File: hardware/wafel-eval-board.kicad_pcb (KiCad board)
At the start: 2 copper layers, 262 parts, among them J101 CAN PORT, J102 SW, J201 Conn_01x02, J202 Conn_01x02, J203 Conn_01x02, J204 Conn_01x02, J205 Conn_01x02, J801 UART1, Q1001 DMG2302UK, Q101 AO3422, Q1101 DMG2302UK, Q1201 DMG2302UK, Q1301 DMG2302UK, Q1401 DMG2302UK, Q1501 DMG2302UK, Q1601 DMG2302UK, Q1701 DMG2302UK, Q1801 DMG2302UK, Q1901 DMG2302UK, Q201 NPN, Q202 DMG2302UK, Q301 IRLML6402, Q302 DMG2302UK, Q401 IPB085N15NM6, Q402 IPB085N15NM6, Q403 IPB085N15NM6, Q501 IPB085N15NM6, Q502 IPB085N15NM6, Q503 IPB085N15NM6, Q601 IRFR9024, Q701 IRFR9024, Q901 ZXMP10A13FTA, Q902 DMG2302UK, SW801 SW_Push, U101 LM5163DDA, U201 BQ7694204, U801 NUCLEO-L432KC, U802 TCAN1043A, U803 TLP241A

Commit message: ADD ZONES
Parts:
- moved D701 5.39 mm to (198.8, 75.7)
- moved R701 5.39 mm to (199.1, 72.7)
- moved D601 0.76 mm to (199.6, 90.9)
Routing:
- added copper zone on B.Cu, net (none)
- added copper zone on F.Cu, net (none)
- added copper zone on B.Cu, net /BAT+
- added copper zone on F.Cu, net /BAT+
- added copper zone on B.Cu, net /CH
- added copper zone on F.Cu, net /CH
- added copper zone on B.Cu, net /PACK+
- added copper zone on F.Cu, net /PACK+
- added copper zone on B.Cu, net PGND
- added copper zone on F.Cu, net PGND
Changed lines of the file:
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@@
 	(footprint "Diode_SMD:D_SOD-123F"
 		(layer "F.Cu")
-		(at 198.7804 81.1052 -90)
+		(at 198.7804 75.7144 -90)
 		(descr "D_SOD-123F")
 		(tags "D_SOD-123F")
@@
 	(footprint "Diode_SMD:D_SOD-123F"
 		(layer "F.Cu")
-		(at 198.882 90.8528 90)
+		(at 199.644 90.9036 90)
 		(descr "D_SOD-123F")
 		(tags "D_SOD-123F")
@@
 	(footprint "Resistor_SMD:R_0603_1608Metric"
 		(layer "F.Cu")
-		(at 199.1238 78.1304)
+		(at 199.1238 72.7396)
 		(descr "Resistor SMD 0603 (1608 Metric), square (rectangular) end terminal, IPC-7351 nominal, (Body size source: IPC-SM-782 page 72, https://www.pcb-3d.com/wordpress/wp-content/uploads/ipc-sm-782a_amendment_1_and_2.pdf)")
 		(tags "resistor")
@@
 	)
 	(zone
+		(net "/BAT+")
+		(layers "F.Cu" "B.Cu")
+		(name "PW_BAT+")
+		(hatch edge 0.5)
+		(priority 1)
+		(connect_pads
+			(clearance 0)
+		)
+		(min_thickness 0.25)
+		(fill
+			(thermal_gap 0.5)
+			(thermal_bridge_width 0.5)
+			(island_removal_mode 1)
+		)
+		(polygon
+			(pts
+				(xy 197.293326 92.960718) (xy 197.188993 137.321792) (xy 268.792701 137.512549) (xy 268.910981 93.17037)
+			)
+		)
+	)
+	(zone
+		(net "/PACK+")
+		(layers "F.Cu" "B.Cu")
+		(name "PW_PACK+")
+		(hatch edge 0.5)
+		(priority 1)
+		(connect_pads
+			(clearance 0)
+		)
+		(min_thickness 0.25)
+		(fill
+			(thermal_gap 0.5)
+			(thermal_bridge_width 0.5)
+			(island_removal_mode 1)
+		)
+		(polygon
+			(pts
+				(xy 197.421911 25.504494) (xy 197.322262 67.874623) (xy 269.213727 68.066145) (xy 269.326697 25.714987)
+			)
+		)
+	)
+	(zone
+		(layers "F.Cu" "B.Cu")
+		(name "PW_BAT-")
+		(hatch edge 0.5)
+		(priority 1)
+		(connect_pads
+			(clearance 0)
+		)
+		(min_thickness 0.25)
+		(fill
+			(thermal_gap 0.5)
+			(thermal_bridge_width 0.5)
+			(island_removal_mode 1)
+		)
+		(polygon
+			(pts
+				(xy 158.3436 91.3892) (xy 158.235467 137.366345) (xy 192.724633 137.458225) (xy 192.84725 91.490204)
+			)
+		)
+	)
+	(zone
+		(net "PGND")
+		(layers "F.Cu" "B.Cu")
+		(name "PW_PACK-")
+		(hatch edge 0.5)
+		(priority 1)
+		(connect_pads
+			(clearance 0)
+		)
+		(min_thickness 0.25)
+		(fill
+			(thermal_gap 0.5)
+			(thermal_bridge_width 0.5)
+			(island_removal_mode 1)
+		)
+		(polygon
+			(pts
+				(xy 158.484756 25.296821) (xy 158.331936 90.274731) (xy 193.004093 90.367098) (xy 193.177392 25.398379)
+			)
+		)
+	)
+	(zone
+		(net "/CH")
+		(layers "F.Cu" "B.Cu")
+		(name "PW_CH")
+		(hatch edge 0.5)
+		(priority 1)
+		(connect_pads
+			(clearance 0)
+		)
+		(min_thickness 0.25)
+		(fill
+			(thermal_gap 0.5)
+			(thermal_bridge_width 0.5)
+			(island_removal_mode 1)
+		)
+		(polygon
+			(pts
+				(xy 209.168977 69.423391) (xy 209.118303 90.969113) (xy 269.152208 91.129048) (xy 269.209638 69.599152)
+			)
+		)
+	)
+	(zone
 		(net "GND")
 		(layers "F.Cu" "B.Cu")
@@
 		(polygon
 			(pts
-				(xy 51.923662 25.302) (xy 51.923662 126.802) (xy 156.7976 126.802) (xy 156.7976 25.302)
+				(xy 51.923662 25.302) (xy 51.923662 137.16) (xy 156.7976 137.16) (xy 156.7976 25.302)
 			)
 		)

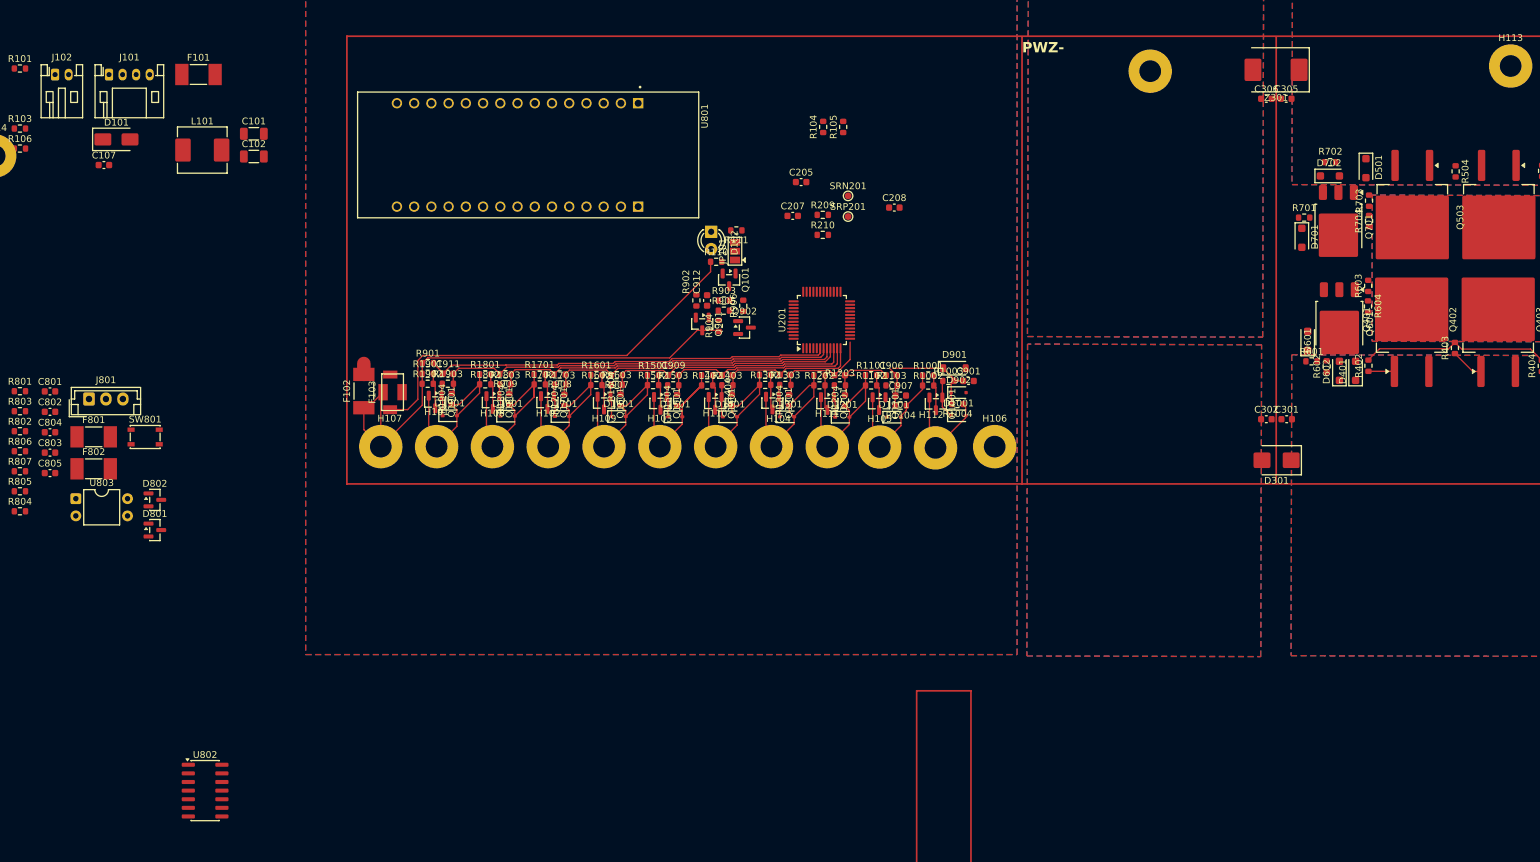
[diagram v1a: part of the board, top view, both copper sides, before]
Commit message: Actualize resistors size
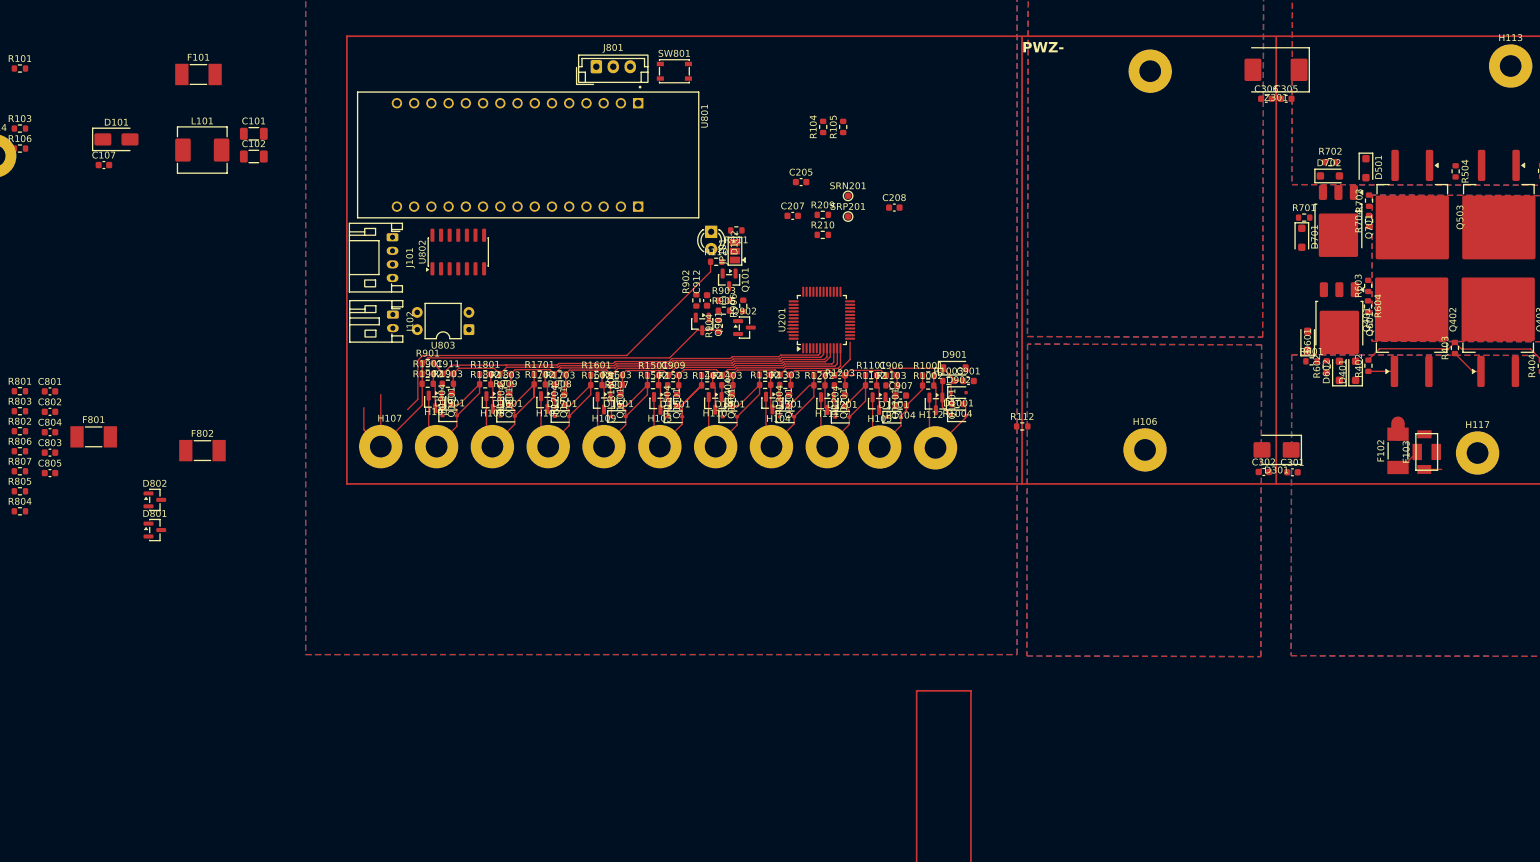
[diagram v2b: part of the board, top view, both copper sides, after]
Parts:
- added H117: BAT+, MountingHole:MountingHole_3.2mm_M3_Pad, F.Cu at (224.7, 107.4)
- added R112: 0, Resistor_SMD:R_0603_1608Metric, F.Cu at (157.6, 103.5)
- moved F103 152.7 mm to (217.2, 107.3)
- moved F102 152.7 mm to (213.0, 107.1)
- moved SW801 94.8 mm to (106.3, 51.2)
- moved J801 89.4 mm to (94.8, 50.5)
- moved U802 87.7 mm to (74.4, 77.8), turned to 90 degrees
- moved U803 63.1 mm to (76.0, 89.3), turned to 180 degrees
- moved J102 61.1 mm to (64.8, 87.0), turned to -90 degrees
- moved J101 48.2 mm to (64.7, 75.6), turned to -90 degrees
- moved H106 22.2 mm to (175.7, 107.0)
- moved F802 16.3 mm to (36.7, 107.1)
- moved C301 7.87 mm to (197.4, 110.3)
- moved C302 7.78 mm to (193.2, 110.2)
- moved D301 1.52 mm to (195.1, 107.0)
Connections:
- F102 pad 1: /CB Mosfets/CELL10 -> Net-(F102-Pad1)
- F103 pad 1: /CB Mosfets/CELL10 -> Net-(F102-Pad1)
- H106 pad 1: GND -> /BAT-
- R202 pad 2: /BAT+ -> /CB Mosfets/VC10
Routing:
- net Net-(F102-Pad1): track 0.00 -> 4.26 mm
- net /CB Mosfets/CELL10: track 79.5 -> 75.3 mm
- added copper zone on B.Cu, net /BAT-
- added copper zone on F.Cu, net /BAT-
- removed copper zone on B.Cu, net (none)
- removed copper zone on F.Cu, net (none)

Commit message: some chnages
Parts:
- D102: footprint LED_THT:LED_D3.0mm -> LED_SMD:LED_0201_0603Metric
- Q1001, Q1101, Q1201, Q1301, Q1401, Q1501, Q1601, Q1701, Q1801, Q1901: value DMG2302UK -> CJ3134K; footprint Package_TO_SOT_SMD:SOT-23 -> Package_TO_SOT_SMD:SOT-723
- Q202, Q302, Q902: value DMG2302UK -> 2N7002K
- R1001, R1002, R1101, R1102, R1201, R1202, R1301, R1302, R1401, R1402, R1501, R1502, R1601, R1602, R1701, R1702, R1801, R1802, R1901, R1902, R603, R604, R703, R704: footprint Resistor_SMD:R_0603_1608Metric -> Resistor_SMD:R_1206_3216Metric
- R104, R105: footprint Resistor_SMD:R_0603_1608Metric -> Resistor_SMD:R_2512_6332Metric
- moved D902 6.57 mm to (149.5, 92.1)
- moved D901 5.62 mm to (150.2, 90.0)
- moved C907 4.89 mm to (144.4, 97.9)
- moved Q1101 4.28 mm to (140.0, 97.8), turned to 180 degrees
- moved Q1001 4.02 mm to (148.4, 98.4), turned to 180 degrees
- moved Q1201 3.64 mm to (131.6, 97.8), turned to 180 degrees
- moved Q1401 3.54 mm to (114.9, 97.7), turned to 180 degrees
- moved R1102 3.26 mm to (136.7, 100.4)
- moved R1002 3.24 mm to (145.1, 100.4)
- moved C906 3.21 mm to (140.8, 94.0)
- moved Q1501 3.20 mm to (106.4, 97.8), turned to 180 degrees
- moved R1103 3.16 mm to (140.8, 95.6)
- moved R1802 3.12 mm to (77.6, 100.3)
- moved Q1301 3.12 mm to (123.2, 98.2), turned to 180 degrees
- moved R1702 3.11 mm to (85.9, 100.4)
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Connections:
- C210 pad 2: GND -> /BAT-
- C302 pad 1: GND -> /BAT-
- D301 pad 2: GND -> /BAT-
- R104 pad 1: GND -> /BAT-
- R105 pad 1: GND -> /BAT-
- R210 pad 2: GND -> /BAT-
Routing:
- net /CB Mosfets/CELL10: track 75.3 -> 0.00 mm
- net /CB Mosfets/VC9: track 60.2 -> 0.00 mm
- net /CB Mosfets/VC10: track 59.7 -> 0.00 mm
- net Net-(F103-Pad4): track 60.6 -> 2.71 mm
- net /CB Mosfets/VC8: track 52.1 -> 0.00 mm
- net /CB Mosfets/VC7: track 44.6 -> 0.00 mm
- net /CB Mosfets/VC6: track 37.1 -> 0.00 mm
- net /CB Mosfets/CELL8: track 30.9 -> 0.00 mm
- net /CB Mosfets/VC5: track 29.6 -> 0.00 mm
- net /CB Mosfets/CELL4: track 28.8 -> 0.00 mm
- net /CB Mosfets/CELL9: track 28.6 -> 0.00 mm
- net /CB Mosfets/CELL7: track 28.1 -> 0.00 mm
- net /CB Mosfets/CELL6: track 28.1 -> 0.00 mm
- net /CB Mosfets/CELL5: track 27.9 -> 0.00 mm
- net /CB Mosfets/CELL3: track 27.6 -> 0.00 mm
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
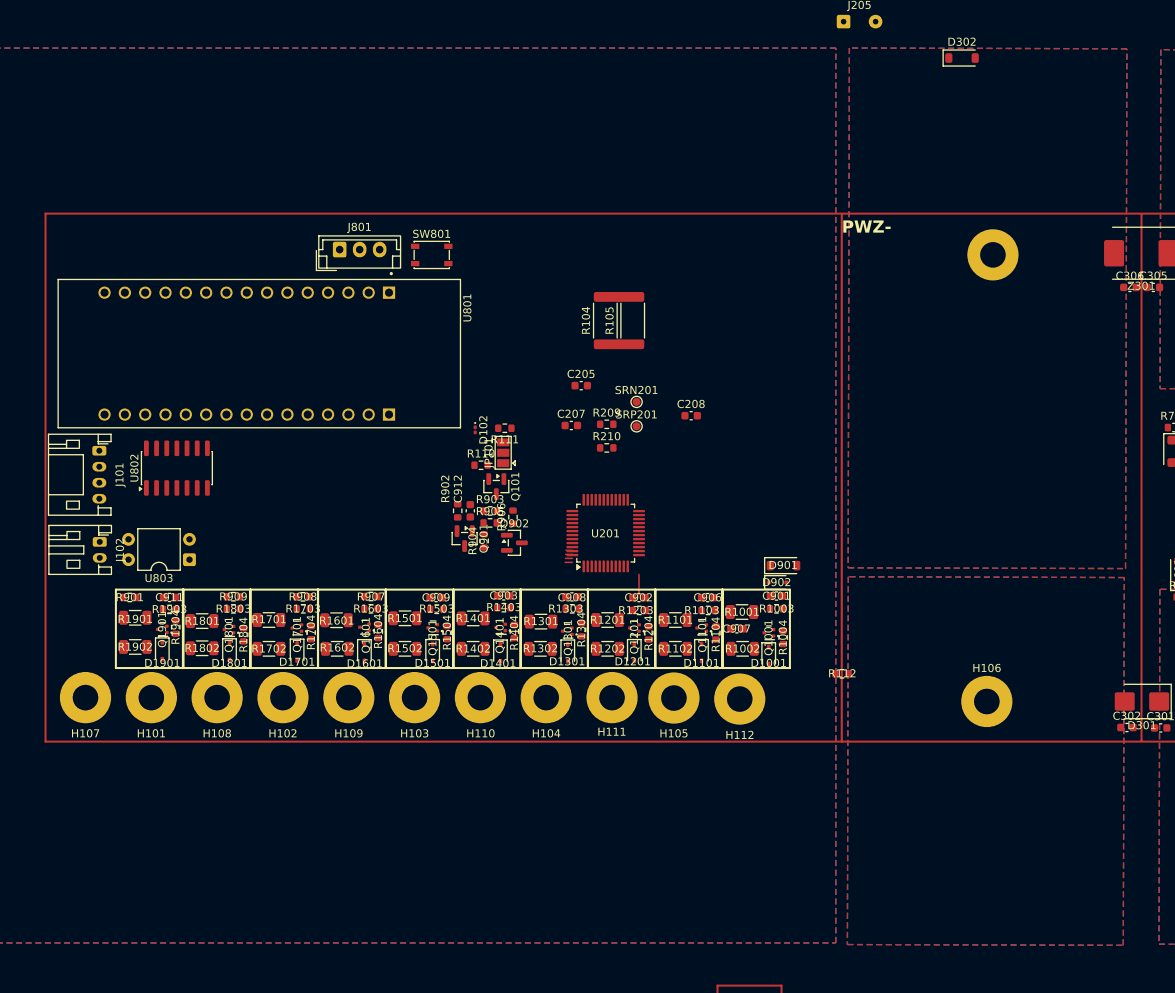
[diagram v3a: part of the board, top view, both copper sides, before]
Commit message: added qulon zone
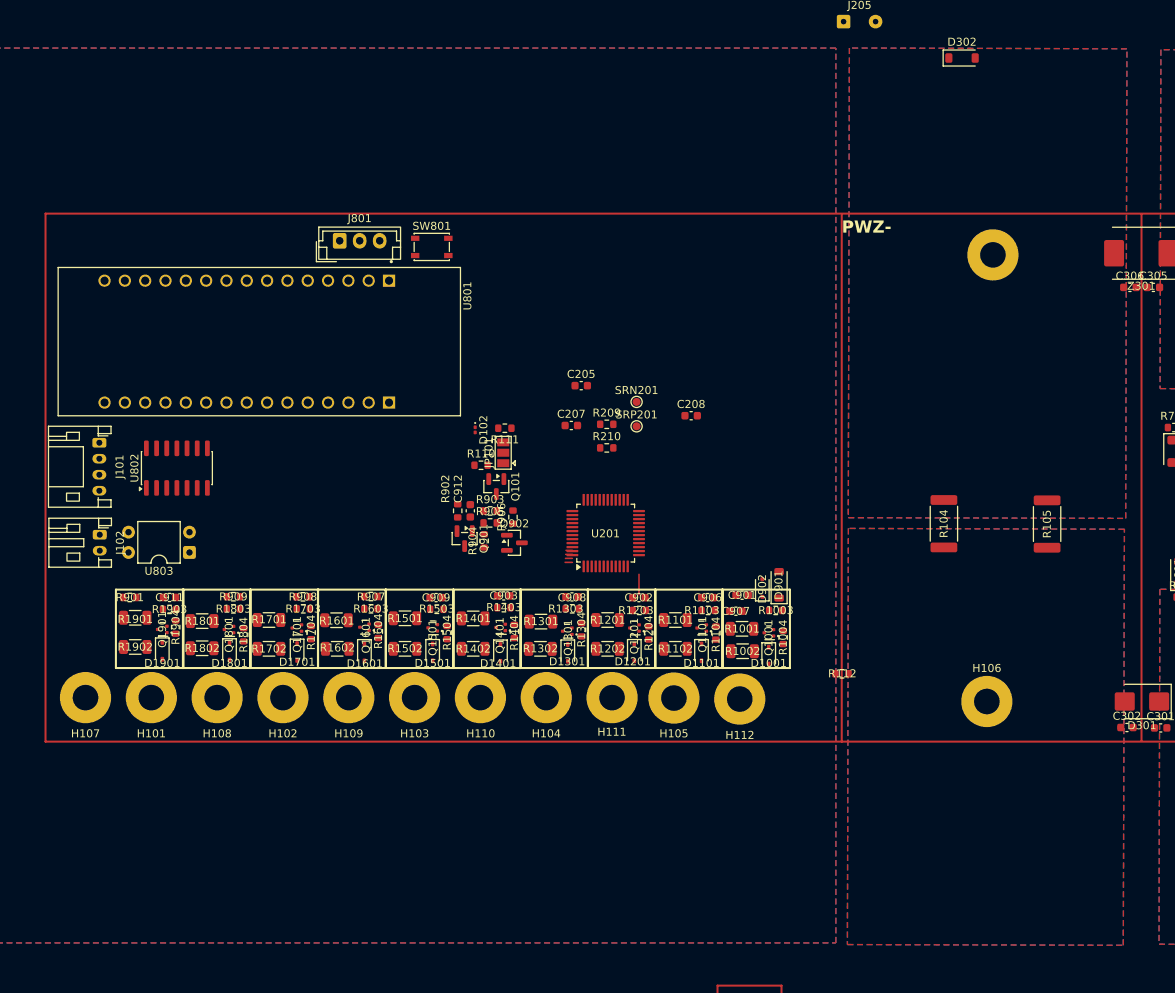
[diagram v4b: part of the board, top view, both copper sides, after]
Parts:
- moved R105 57.9 mm to (183.2, 84.8)
- moved R104 49.2 mm to (170.3, 84.8)
- moved C901 4.30 mm to (145.1, 93.7), turned to 180 degrees
- moved D901 2.46 mm to (149.7, 92.4), turned to 90 degrees
- moved C907 2.20 mm to (144.3, 95.7)
- moved R1001 2.10 mm to (145.1, 97.9)
- moved D902 2.02 mm to (147.6, 92.8), turned to 90 degrees
- moved U801 1.50 mm to (84.7, 62.0)
- moved J801 1.10 mm to (94.8, 49.4)
- moved J101 1.00 mm to (64.7, 74.6)
- moved SW801 1.00 mm to (106.3, 50.2)
- moved J102 0.90 mm to (64.8, 86.1)
- moved U803 0.90 mm to (76.0, 88.4)
- moved R1002 0.30 mm to (145.1, 100.7)
- moved R1003 0.22 mm to (149.3, 95.6)

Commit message: Update C301-C306 to 1206 100V capacitors
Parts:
- C301, C302, C303, C304, C305, C306: footprint Capacitor_SMD:C_0603_1608Metric -> Capacitor_SMD:C_1206_3216Metric
- moved R312 224.8 mm to (297.0, 34.4)
- moved R303 198.0 mm to (258.8, 38.5)
- moved R304 198.0 mm to (258.8, 41.5)
- moved R309 198.0 mm to (267.6, 32.6)
- moved R310 198.0 mm to (267.6, 35.5)
- moved R311 198.0 mm to (267.6, 38.5)
- moved D303 198.0 mm to (258.2, 18.7)
- moved D304 198.0 mm to (275.8, 18.6)
- moved D305 198.0 mm to (270.1, 18.6)
- moved D306 198.0 mm to (270.1, 21.9)
- moved D308 198.0 mm to (270.1, 25.3)
- moved D309 198.0 mm to (270.1, 28.6)
- moved D310 198.0 mm to (258.2, 22.2)
- moved D311 198.0 mm to (258.2, 25.8)
- moved D312 198.0 mm to (258.2, 29.4)
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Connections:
- net Net-(F102-Pad1) renamed /xBAT+
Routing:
- net /xBAT+: track 4.26 -> 0.00 mm
- net Net-(Q401-G): track 3.89 -> 0.03 mm
- net Net-(F103-Pad4): track 2.71 -> 0.00 mm
- net /High-Side N-MOSFET/MOSFET-CASCADE-CHG/GATE: track 27.8 -> 25.4 mm
- net /BAT+: track 1.61 -> 0.00 mm
- added copper zone on B.Cu, net /xBAT+
- added copper zone on F.Cu, net /xBAT+
